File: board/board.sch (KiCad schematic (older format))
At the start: 71 parts, among them U2 10M02SCE144

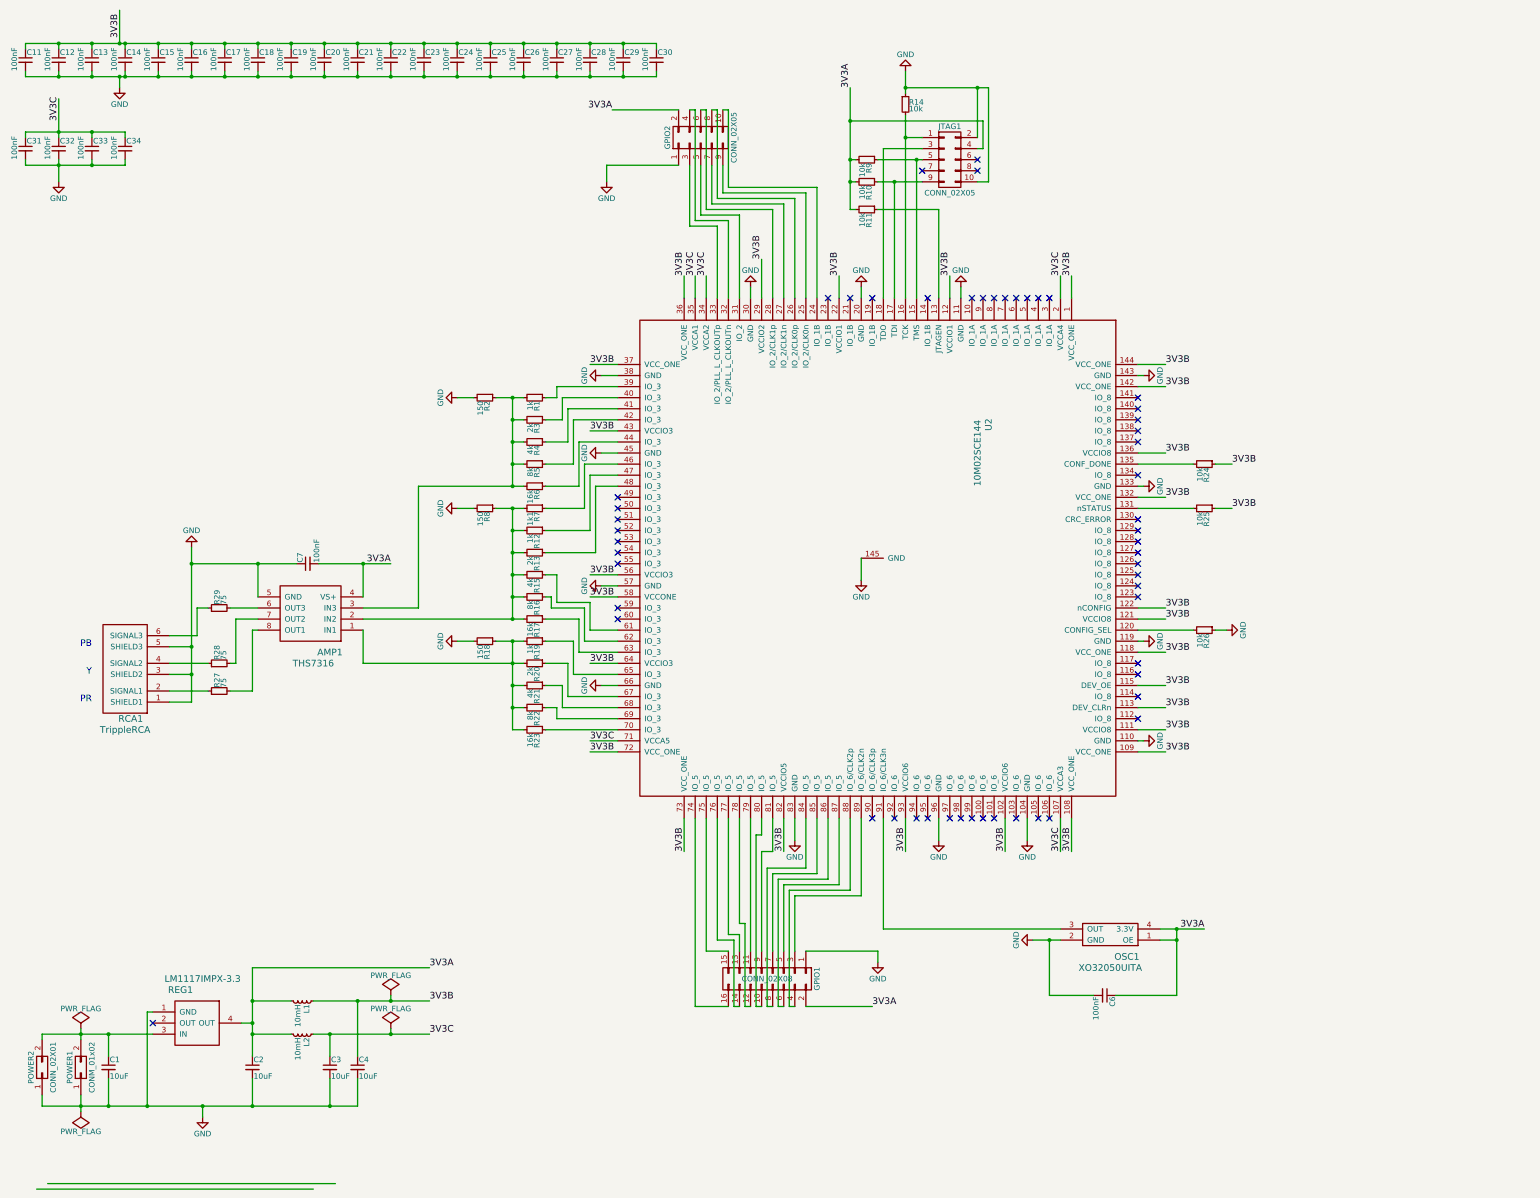
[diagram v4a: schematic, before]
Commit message: Complete redo of the board
In Rev.1 I got GND and Line mixed up for the Video line sockets. As I
had to modify the board anyway, I also changed the location of the FPGA
from backside to front side and therefore had to redo everything.
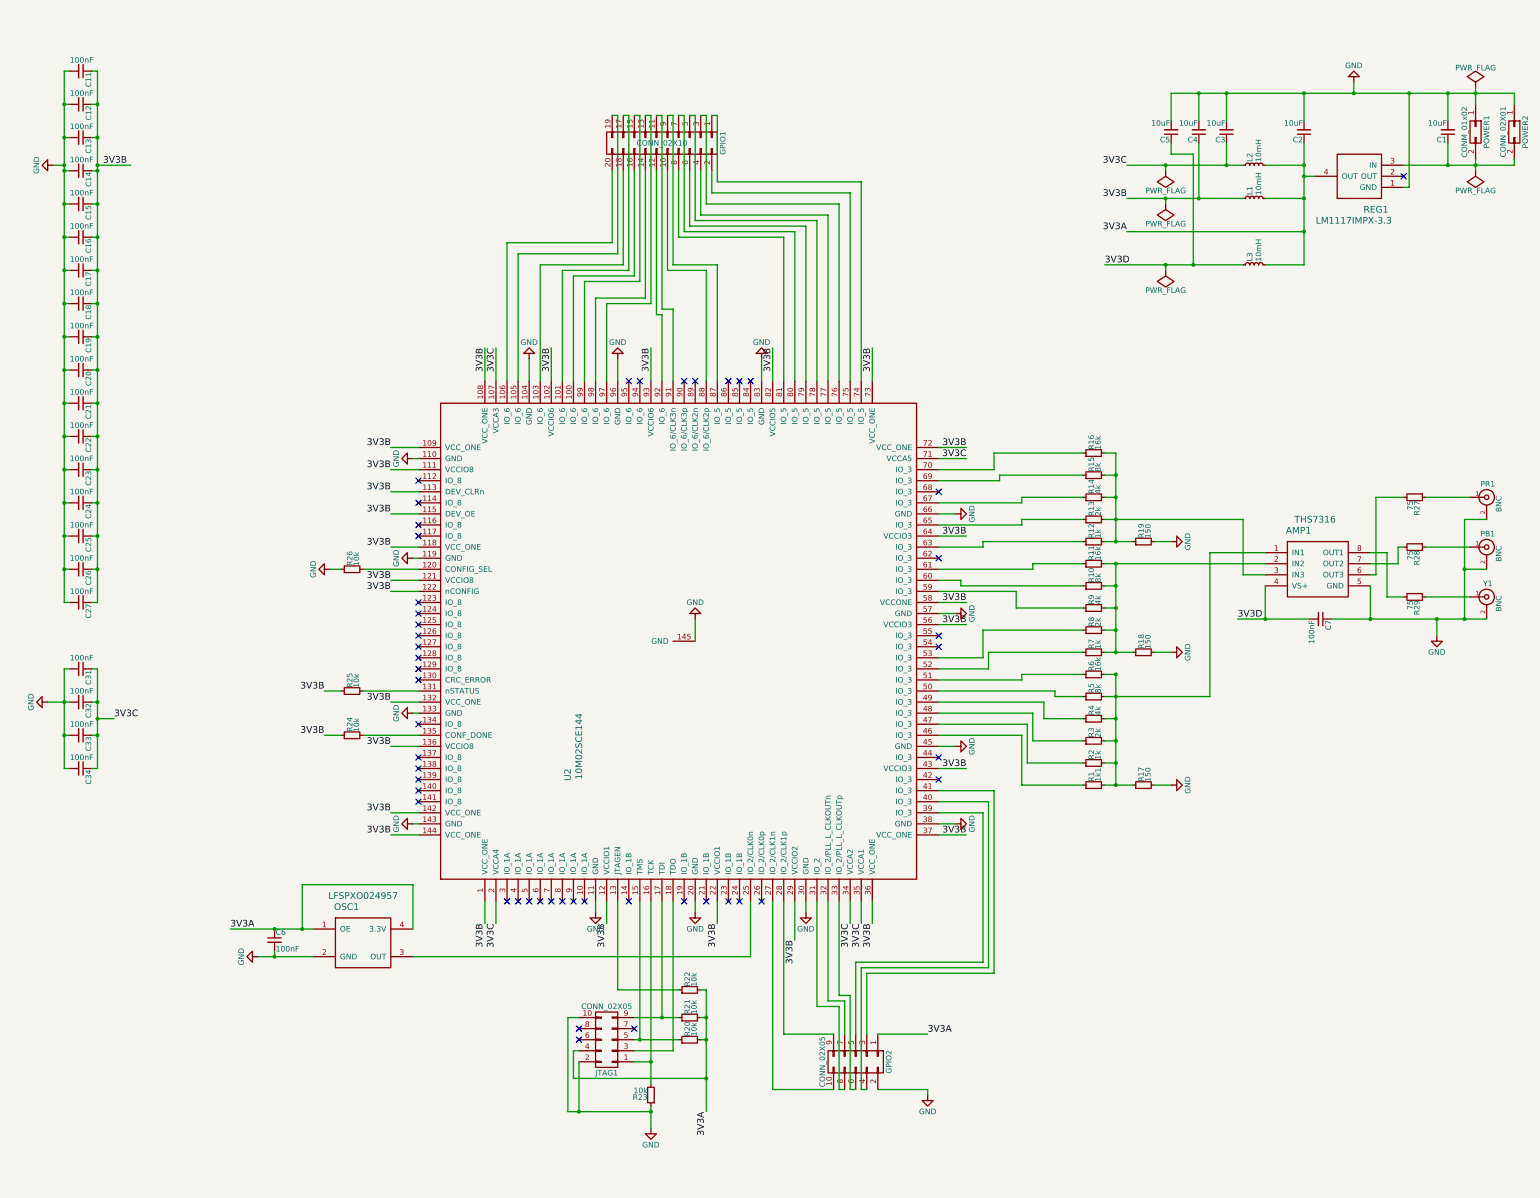
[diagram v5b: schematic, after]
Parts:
- removed C28, C29, C30: 100nF, Capacitors_SMD:C_0603_HandSoldering, symbol C_Small
- removed GPIO1: CONN_02X08, Pin_Headers:Pin_Header_Straight_2x08_Pitch2.54mm, symbol CONN_02X08
- removed OSC1: XO32050UITA, Oscillators:Oscillator_SMD_EuroQuartz_XO32-4pin_3.2x2.5mm_HandSoldering, symbol XO32050UITA
- removed RCA1: TrippleRCA, footprints:TrippleRCA, symbol TrippleRCA
- added C5: 10uF, Capacitors_SMD:C_0805_HandSoldering, symbol C_Small
- added GPIO1: CONN_02X10, Pin_Headers:Pin_Header_Straight_2x10_Pitch2.54mm, symbol CONN_02X10
- added L3: 10mH, Capacitors_SMD:C_0805_HandSoldering, symbol L_Small
- added OSC1: LFSPXO024957, Oscillators:Oscillator_SMD_EuroQuartz_XO53-4pin_5.0x3.2mm_HandSoldering, symbol LFSPXO024957
- added PB1, PR1, Y1: BNC, footprints:RCA_JACK, symbol BNC
- R1: value 1k -> 1k1
- R2: renamed from R3; value 2k -> 1k
- R3: renamed from R4; value 4k -> 2k
- R4: renamed from R5; value 8k -> 4k
- R5: renamed from R6; value 16k -> 8k
- R6: renamed from R7; value 1k1 -> 16k
- renumbered R16 to R10, R17 to R11, R19 to R12, R20 to R13, R21 to R14, R22 to R15, R23 to R16, R2 to R17, R8 to R18, R18 to R19, R9 to R20, R10 to R21, R11 to R22, R14 to R23, R12 to R7, R13 to R8, R15 to R9
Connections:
- net 3V3A: now also GPIO2.1 (P1), L3.2, OSC1.1 (OE), OSC1.4 (3.3V); no longer AMP1.4 (VS+), C7.2, GPIO2.2 (P2)
- net GND: now also GPIO2.2 (P2), C5.2, OSC1.2 (GND), PB1.2 (Ext), PR1.2 (Ext), Y1.2 (Ext); no longer GPIO2.1 (P1)
- net at U2.100 (IO_6): now also GPIO1.16 (P16)
- net at U2.101 (IO_6): now also GPIO1.17 (P17)
- net at U2.103 (IO_6): now also GPIO1.18 (P18)
- net at U2.105 (IO_6): now also GPIO1.19 (P19)
- net at U2.106 (IO_6): now also GPIO1.20 (P20)
- net at U2.24 (IO_1B): no longer GPIO2.10 (P10)
- net at U2.25 (IO_2/CLK0n): now also OSC1.3 (OUT); no longer GPIO2.9 (P9)
- net at U2.26 (IO_2/CLK0p): no longer GPIO2.8 (P8)
- net at U2.27 (IO_2/CLK1n): now also GPIO2.10 (P10); no longer GPIO2.7 (P7)
- net at U2.28 (IO_2/CLK1p): now also GPIO2.9 (P9); no longer GPIO2.6 (P6)
- net at U2.31 (IO_2): now also GPIO2.8 (P8); no longer GPIO2.5 (P5)
- net at U2.32 (IO_2/PLL_L_CLKOUTn): now also GPIO2.7 (P7); no longer GPIO2.4 (P4)
- net at U2.33 (IO_2/PLL_L_CLKOUTp): now also GPIO2.6 (P6); no longer GPIO2.3 (P3)
- net at U2.39 (IO_3): now also GPIO2.5 (P5); no longer R1.1
- net at U2.40 (IO_3): now also GPIO2.4 (P4); no longer R2.1
- net at U2.41 (IO_3): now also GPIO2.3 (P3); no longer R3.1
- net at U2.42 (IO_3): no longer R4.1
- net at U2.44 (IO_3): no longer R5.1
- net at U2.46 (IO_3): now also R1.1; no longer R6.1
- net at U2.47 (IO_3): now also R2.1; no longer R7.1
- net at U2.48 (IO_3): now also R3.1; no longer R8.1
- net at U2.49 (IO_3): now also R4.1
- net at U2.50 (IO_3): now also R5.1
- net at U2.51 (IO_3): now also R6.1
- net at U2.52 (IO_3): now also R7.1
- net at U2.53 (IO_3): now also R8.1
- net at U2.59 (IO_3): now also R9.1
- net at U2.60 (IO_3): now also R10.1
- net at U2.61 (IO_3): now also R11.1; no longer R9.1
- net at U2.62 (IO_3): no longer R10.1
- net at U2.63 (IO_3): now also R12.1; no longer R11.1
- net at U2.65 (IO_3): now also R13.1; no longer R12.1
- net at U2.67 (IO_3): now also R14.1; no longer R13.1
- net at U2.68 (IO_3): no longer R14.1
- net at U2.74 (IO_5): now also GPIO1.1 (P1)
- net at U2.75 (IO_5): now also GPIO1.2 (P2)
- net at U2.76 (IO_5): now also GPIO1.3 (P3)
- net at U2.77 (IO_5): now also GPIO1.4 (P4)
- net at U2.78 (IO_5): now also GPIO1.5 (P5)
- net at U2.79 (IO_5): now also GPIO1.6 (P6)
- net at U2.80 (IO_5): now also GPIO1.7 (P7)
- net at U2.81 (IO_5): now also GPIO1.8 (P8)
- net at U2.87 (IO_5): now also GPIO1.9 (P9)
- net at U2.88 (IO_6/CLK2p): now also GPIO1.10 (P10)
- net at U2.91 (IO_6/CLK3n): now also GPIO1.11 (P11)
- net at U2.92 (IO_6): now also GPIO1.12 (P12)
- net at U2.97 (IO_6): now also GPIO1.13 (P13)
- net at U2.98 (IO_6): now also GPIO1.14 (P14)
- net at U2.99 (IO_6): now also GPIO1.15 (P15)
- net at R12.2, R13.2, R14.2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: now also AMP1.3 (IN3); no longer AMP1.1 (IN1)
- net at AMP1.2 (IN2), R10.2, R11.2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: no longer R6.2
- net at R1.2, R17.1, R2.2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: now also AMP1.1 (IN1), R6.2; no longer AMP1.3 (IN3)
- net at AMP1.6 (OUT3): now also R27.2; no longer R29.2
- net at AMP1.8 (OUT1): now also R29.2; no longer R27.2
- net at R29.1: now also Y1.1 (In)
- net at R28.1: now also PB1.1 (In)
- net at R27.1: now also PR1.1 (In)
- new net 3V3D: AMP1.4 (VS+), C5.1, C7.2, L3.1
- no-connect marks 55 -> 49
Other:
- note removed: "PB"
- note removed: "PR"
- note removed: "Y"
- moved on the sheet: AMP1, C1, C11, C12, C13, C14, C15, C16, C17, C18, C19, C2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

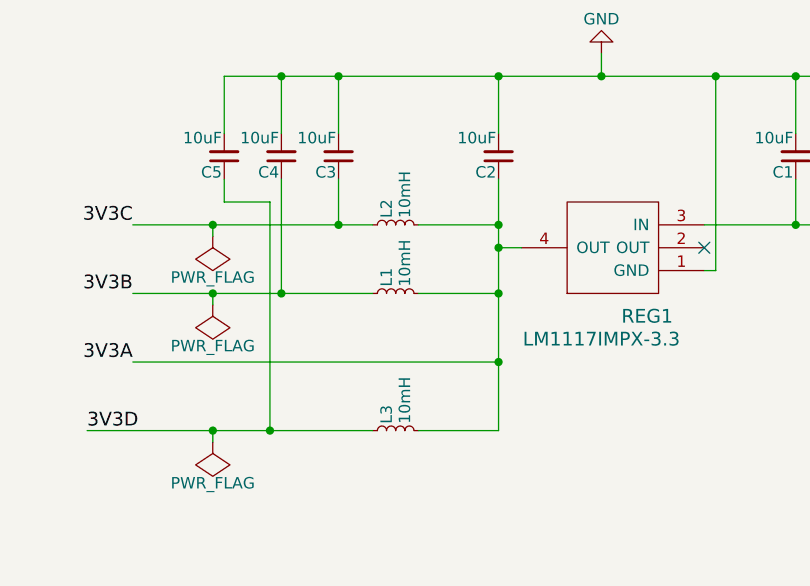
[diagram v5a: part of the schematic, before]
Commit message: Modifed programs for A-Video Board Rev.2
Finally got the PCB for the Rev.2. Assembled the board and everything
worked at first try  :-)
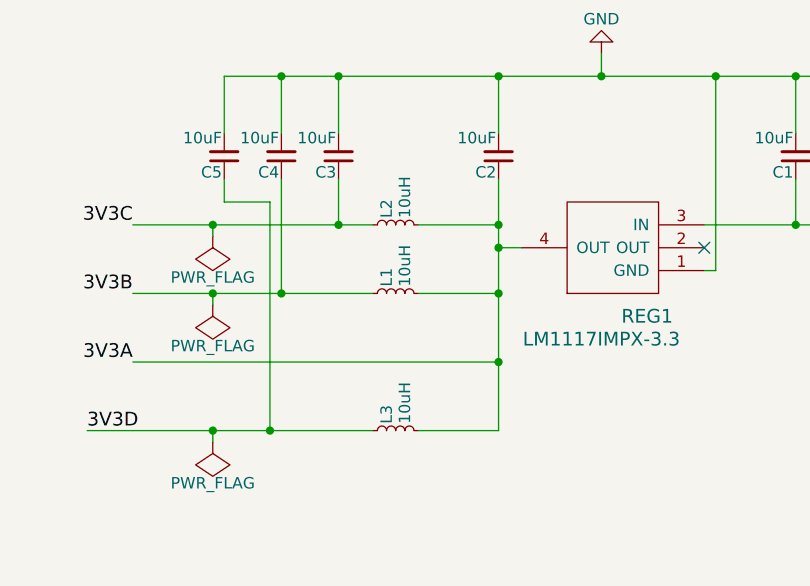
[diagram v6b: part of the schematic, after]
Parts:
- L1, L2, L3: value 10mH -> 10uH
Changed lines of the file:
@@
 P 11800 1950
 F 0 "L2" H 11830 1990 50  0000 L CNN
-F 1 "10mH" H 11830 1910 50  0000 L CNN
+F 1 "10uH" H 11830 1910 50  0000 L CNN
 F 2 "Capacitors_SMD:C_0805_HandSoldering" H 11800 1950 50  0001 C CNN
 F 3 "" H 11800 1950 50  0000 C CNN
@@
 P 11800 2250
 F 0 "L1" H 11830 2290 50  0000 L CNN
-F 1 "10mH" H 11830 2210 50  0000 L CNN
+F 1 "10uH" H 11830 2210 50  0000 L CNN
 F 2 "Capacitors_SMD:C_0805_HandSoldering" H 11800 2250 50  0001 C CNN
 F 3 "" H 11800 2250 50  0000 C CNN
@@
 P 11800 2850
 F 0 "L3" H 11830 2890 50  0000 L CNN
-F 1 "10mH" H 11830 2810 50  0000 L CNN
+F 1 "10uH" H 11830 2810 50  0000 L CNN
 F 2 "Capacitors_SMD:C_0805_HandSoldering" H 11800 2850 50  0001 C CNN
 F 3 "" H 11800 2850 50  0000 C CNN
